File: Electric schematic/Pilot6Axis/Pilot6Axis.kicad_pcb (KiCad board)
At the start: 2 copper layers, 74 x 54 mm, 111 parts, among them IC1 LM27313XMFX_NOPB, IC3 BQ25792RQMR, IC4 TPS25751SRSMR, J1 Battery input, J10 BTN5, J11 BTN6, J12 BTN7, J13 BTN8, J14 BTN9, J15 Power switch, J16 Oled, J19 Conn_02x03_Odd_Even, J2 USB_C_Receptacle_USB2.0_16P, J3 Conn_02x03_Odd_Even, J5 Oled, J6 BTN1, J7 BTN2, J8 BTN3, J9 BTN4, Q1 S9014, Q2 AO3400A, Q3 S9014, Q4 AO3400A, SW1 SW_Push, SW2 SW_Push, U1 AMS1117-3.3, U2 USBLC6-2SC6, U3 CP2102N-Axx-xQFN28, U4 ESP32-WROOM-32U

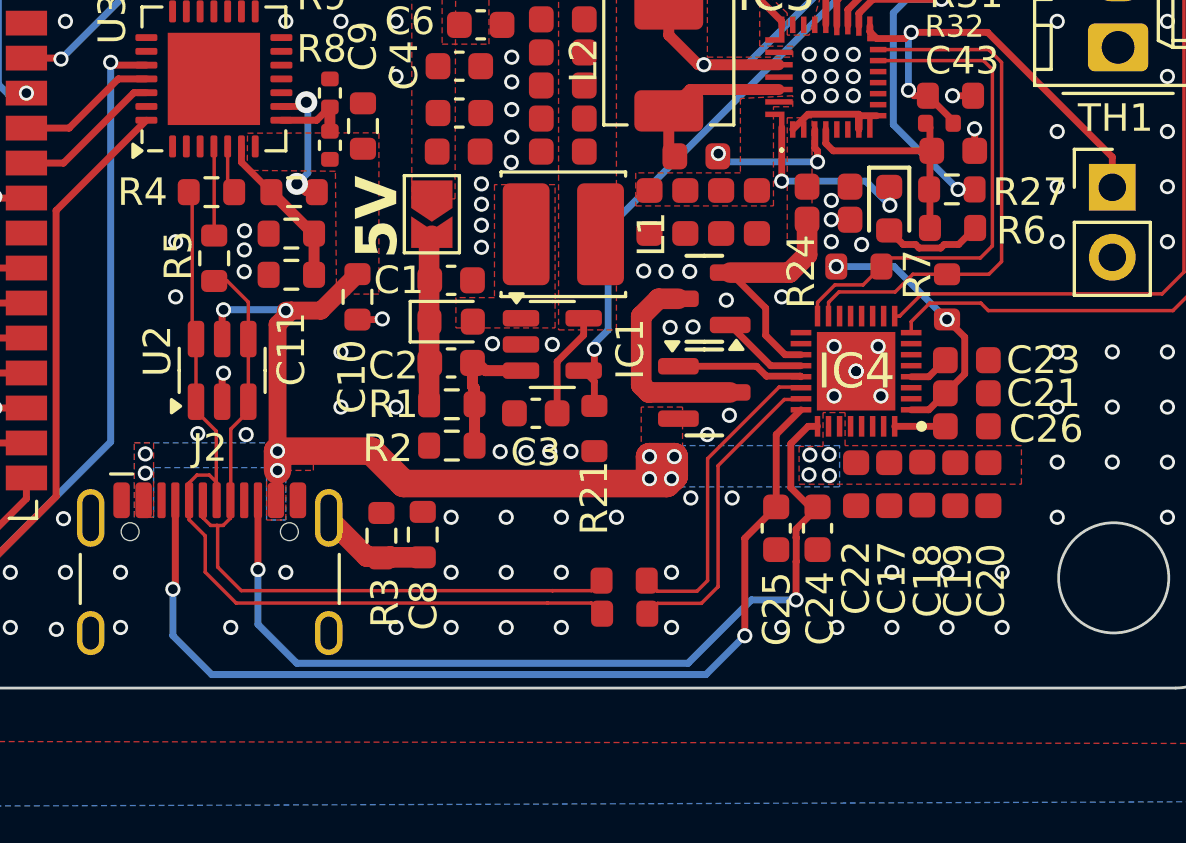
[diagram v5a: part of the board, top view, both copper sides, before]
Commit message: [pd] added 5V to PD
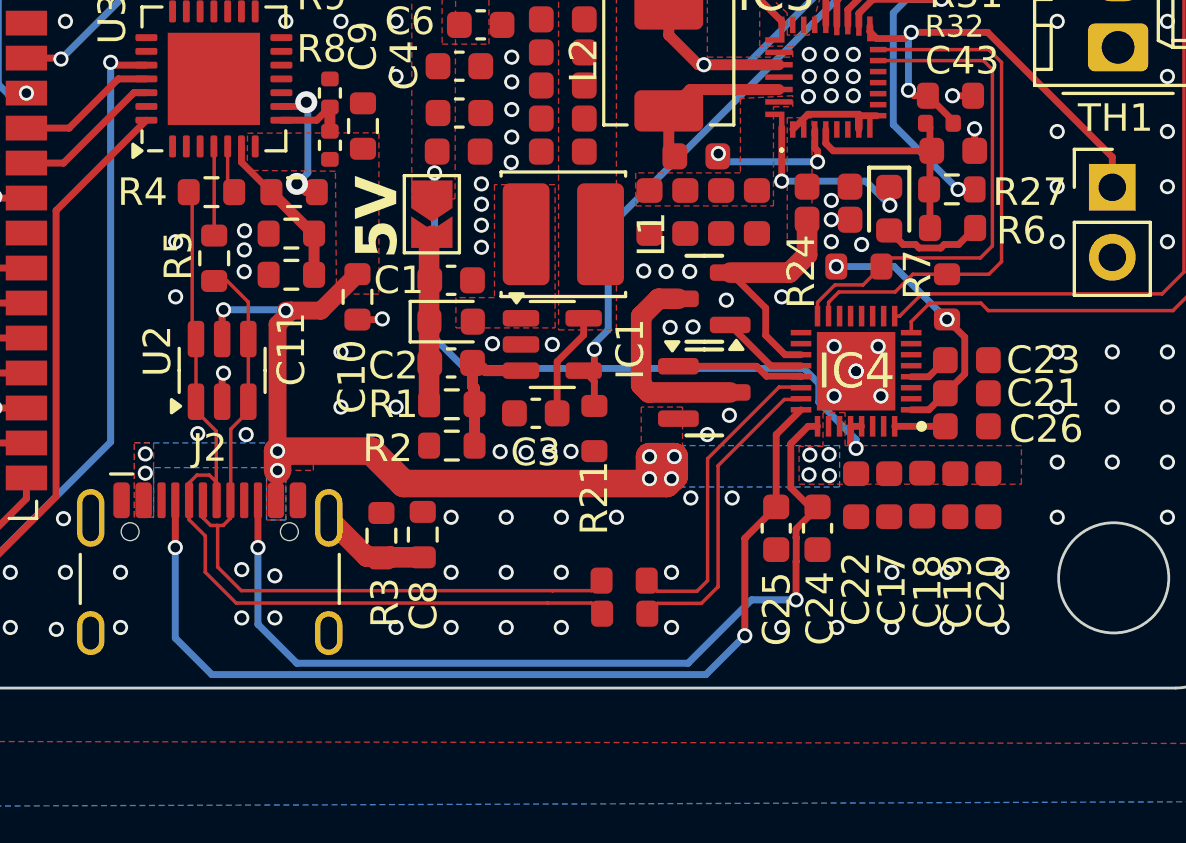
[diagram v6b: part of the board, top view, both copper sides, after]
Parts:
- moved C17 0.40 mm to (176.7, 118.6)
- moved C18 0.40 mm to (177.9, 118.6)
- moved C19 0.40 mm to (179.1, 118.6)
- moved C20 0.40 mm to (180.3, 118.6)
- moved C22 0.40 mm to (175.5, 118.6)
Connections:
- IC4 pad 28: unconnected-(IC4-PP5V_1-Pad28) -> +5V
- IC4 pad 29: unconnected-(IC4-PP5V_2-Pad29) -> +5V
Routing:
- net +5V: track 0.00 -> 24.8 mm, vias 0 -> 2
- net GND: vias 394 -> 396

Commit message: fixed leyout
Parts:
- removed C13: 1nF, Capacitor_SMD:C_0603_1608Metric
- removed C3: 2.2uF, Capacitor_SMD:C_0603_1608Metric
- removed R14: 470R, Resistor_SMD:R_0603_1608Metric
- removed R17, R18: 22Ω, PCM_JLCPCB:R_0603
- added R26: 22Ω, PCM_JLCPCB:R_0603, F.Cu at (123.4, 101.0)
- C35, C36: moved to B.Cu
- R13: value 470R -> 22Ω; footprint Resistor_SMD:R_0603_1608Metric -> PCM_JLCPCB:R_0603
- moved C36 4.73 mm to (173.2, 101.7), turned to 180 degrees
- moved C35 3.42 mm to (172.9, 105.1)
- moved C45 2.47 mm to (170.6, 96.4), turned to 90 degrees
- moved C37 2.33 mm to (171.8, 96.4), turned to 90 degrees
- moved C30 2.28 mm to (173.9, 97.6), turned to 180 degrees
- moved C29 2.06 mm to (173.9, 96.4), turned to 180 degrees
- moved C24 1.27 mm to (173.2, 120.7), turned to 180 degrees
- moved R30 1.10 mm to (176.3, 98.3)
- moved R21 1.05 mm to (165.2, 115.5), turned to 180 degrees
- moved C25 0.85 mm to (173.2, 119.2), turned to 180 degrees
- moved C31 0.22 mm to (169.3, 108.1)
- moved C32 0.22 mm to (168.0, 108.1)
- moved C33 0.22 mm to (171.9, 108.1)
- moved C34 0.22 mm to (170.6, 108.1)
- turned R13 to 0 degrees
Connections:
- C14 pad 2: Net-(C14-Pad2) -> /MCU/IO0
- IC4 pad 22: /PD/PD_D+ -> unconnected-(IC4-GPIO4/USB_P/LD1-Pad22)
- IC4 pad 23: /PD/PD_D- -> unconnected-(IC4-GPIO5/USB_N/LD2-Pad23)
- SW2 pad 2: Net-(C14-Pad2) -> Net-(R26-Pad1)
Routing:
- net /USB/USB_CONN_D-: track 32.0 -> 14.1 mm
- net /USB/USB_CONN_D+: track 27.6 -> 11.6 mm
- net /PD/PD_D+: track 11.4 -> 0.00 mm
- net /PD/PD_D-: track 11.4 -> 0.00 mm
- net Net-(C14-Pad2): track 9.49 -> 0.00 mm
- net /Power/VPOWER_ENABLE: track 31.8 -> 41.1 mm
- net /PD/SW2: track 14.5 -> 7.29 mm, vias 2 -> 1
- net /PD/CC1: track 35.9 -> 29.7 mm, vias 2 -> 0
- net /PD/CC2: track 33.3 -> 28.3 mm
- net Net-(R26-Pad1): track 0.00 -> 3.98 mm
- net Net-(R13-Pad1): track 7.78 -> 3.93 mm
- net /PD/VCC_OUT: track 26.1 -> 22.4 mm
- net /PD/BTST1: track 5.05 -> 2.19 mm, vias 2 -> 1
- net /MCU/EN: track 19.6 -> 21.9 mm
- net /PD/PROG: track 2.74 -> 3.97 mm
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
